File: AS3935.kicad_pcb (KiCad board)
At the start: 2 copper layers, 53.8 x 46.2 mm, 16 parts, among them IC1 AS3935-BQFT, J1 Power, J2 A1, J3 A0, J4 Conn_01x02_Male, J5 Conn_01x03_Male, J6 Conn_01x02_Male, J7 Conn_01x05_Male

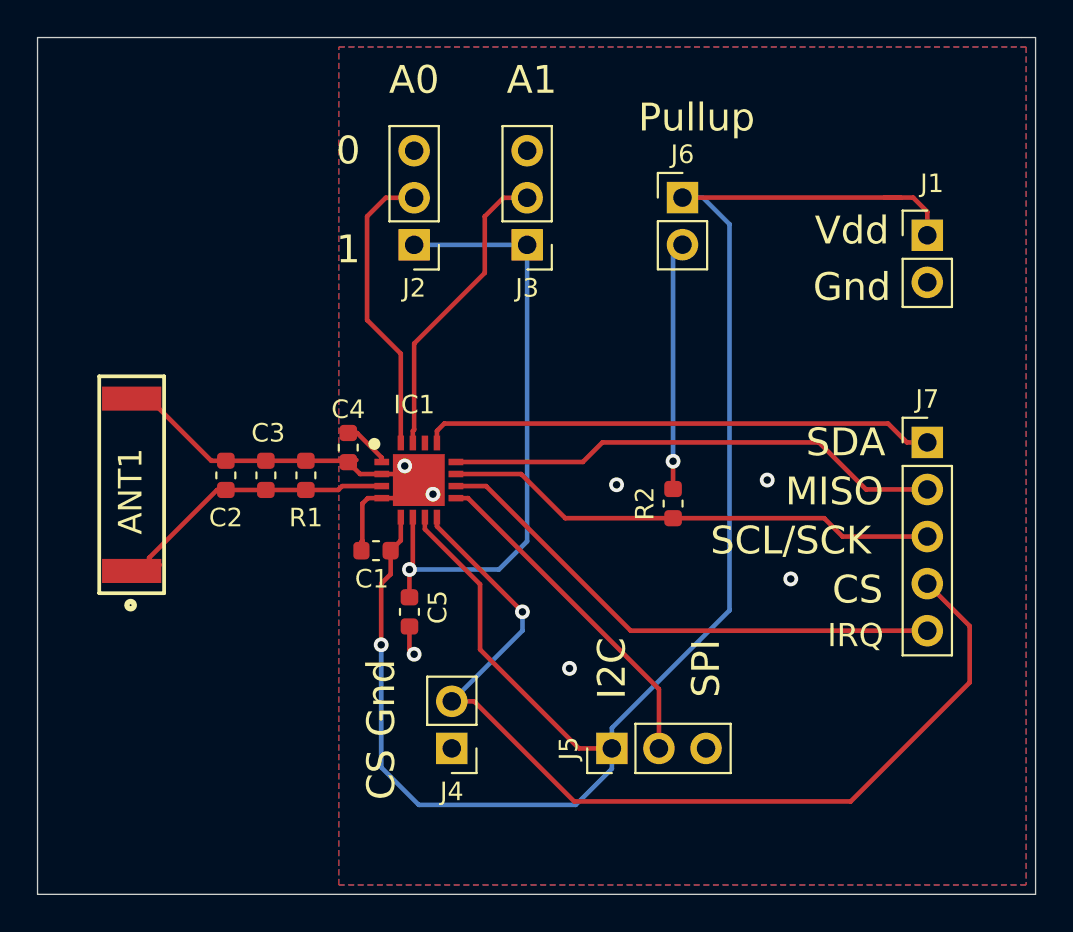
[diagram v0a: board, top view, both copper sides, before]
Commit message: Added IRQ LED
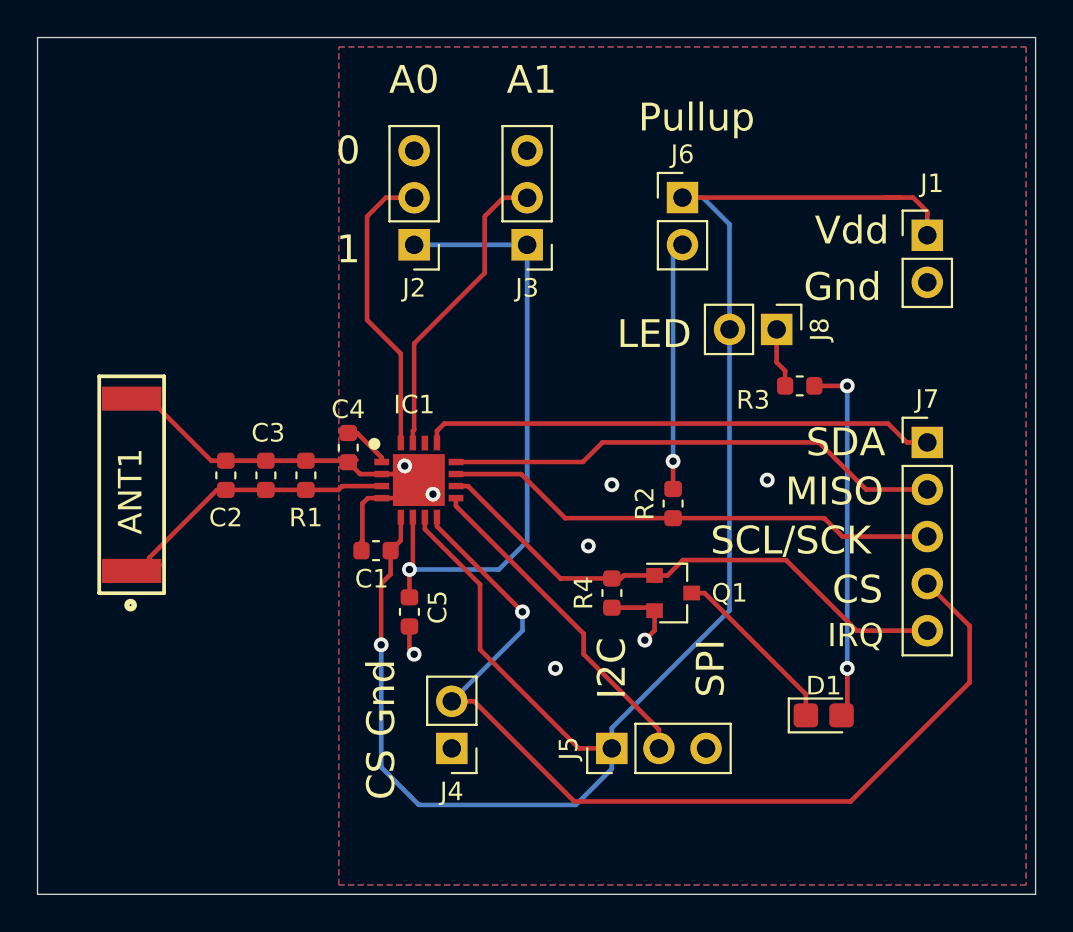
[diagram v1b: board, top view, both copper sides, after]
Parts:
- added D1: LED, LED_SMD:LED_0805_2012Metric_Castellated, F.Cu at (136.4, 84.8)
- added J8: Conn_01x02_Male, Connector_PinHeader_2.54mm:PinHeader_1x02_P2.54mm_Vertical, F.Cu at (133.9, 64.0)
- added Q1: 2N7002K, Package_TO_SOT_SMD:SOT-23, F.Cu at (128.3, 78.2)
- added R3: 150, Resistor_SMD:R_0603_1608Metric, F.Cu at (135.1, 67.1)
- added R4: 10 K, Resistor_SMD:R_0603_1608Metric, F.Cu at (125.0, 78.2)
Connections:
- net Net-(IC1-Pad10) renamed /IRQ
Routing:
- net Net-(D1-Pad2): track 0.00 -> 19.7 mm, vias 0 -> 2
- net Net-(D1-Pad1): track 0.00 -> 9.57 mm
- net GND: track 26.9 -> 31.1 mm, vias 7 -> 8
- net Net-(J8-Pad1): track 0.00 -> 3.24 mm
- net /IRQ: track 28.7 -> 29.5 mm
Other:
- board text added: "LED"

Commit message: Added JLC serial
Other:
- board text added: "JLCJLCJLCJLC"
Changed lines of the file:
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@@
   (general
     (thickness 1.6)
-    (drawings 24)
+    (drawings 25)
     (tracks 160)
     (zones 0)
@@
       (net 2 "Net-(ANT1-Pad1)"))
   )
+  (gr_text JLCJLCJLCJLC (at 141.732 92.964) (layer B.SilkS)
+    (effects (font (size 0.8 0.8) (thickness 0.15)) (justify mirror))
+  )
   (gr_text LED (at 127.254 64.262) (layer F.SilkS)

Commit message: Final pcb
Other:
- rule pad_to_mask_clearance: 0.051 -> 0.05
- rule solder_mask_min_width: 0.25 -> 0.2
